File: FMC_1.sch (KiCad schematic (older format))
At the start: 14 parts, among them J5 SAMTEC_ASP-134603-01

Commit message: bugs fixed, silkscreen edited
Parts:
- renumbered J5 to P1
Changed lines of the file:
@@
 $EndComp
 $Comp
-L SAMTEC:SAMTEC_ASP-134603-01 J5
+L SAMTEC:SAMTEC_ASP-134603-01 P1
 U 1 1 5CF32820
 P 3750 1550
-F 0 "J5" H 4077 -500 50  0000 L CNN
+F 0 "P1" H 4077 -500 50  0000 L CNN
 F 1 "SAMTEC_ASP-134603-01" H 3750 -2640 60  0001 L CNN
 F 2 "SAMTEC_ASP-134603-01" H 3750 -3540 60  0001 L CNN
@@
 $EndComp
 $Comp
-L SAMTEC:SAMTEC_ASP-134603-01 J5
+L SAMTEC:SAMTEC_ASP-134603-01 P1
 U 2 1 5CF32A89
 P 6050 1550
-F 0 "J5" H 6378 -500 50  0000 L CNN
+F 0 "P1" H 6378 -500 50  0000 L CNN
 F 1 "SAMTEC_ASP-134603-01" H 6050 -2640 60  0001 L CNN
 F 2 "SAMTEC_ASP-134603-01" H 6050 -3540 60  0001 L CNN
@@
 $EndComp
 $Comp
-L SAMTEC:SAMTEC_ASP-134603-01 J5
+L SAMTEC:SAMTEC_ASP-134603-01 P1
 U 3 1 5CF32CEE
 P 8800 1550
-F 0 "J5" H 9128 -500 50  0000 L CNN
+F 0 "P1" H 9128 -500 50  0000 L CNN
 F 1 "SAMTEC_ASP-134603-01" H 8800 -2640 60  0001 L CNN
 F 2 "SAMTEC_ASP-134603-01" H 8800 -3540 60  0001 L CNN
@@
 $EndComp
 $Comp
-L SAMTEC:SAMTEC_ASP-134603-01 J5
+L SAMTEC:SAMTEC_ASP-134603-01 P1
 U 4 1 5CF32F53
 P 11450 1550
-F 0 "J5" H 11778 -500 50  0000 L CNN
+F 0 "P1" H 11778 -500 50  0000 L CNN
 F 1 "SAMTEC_ASP-134603-01" H 11450 -2640 60  0001 L CNN
 F 2 "SAMTEC_ASP-134603-01" H 11450 -3540 60  0001 L CNN

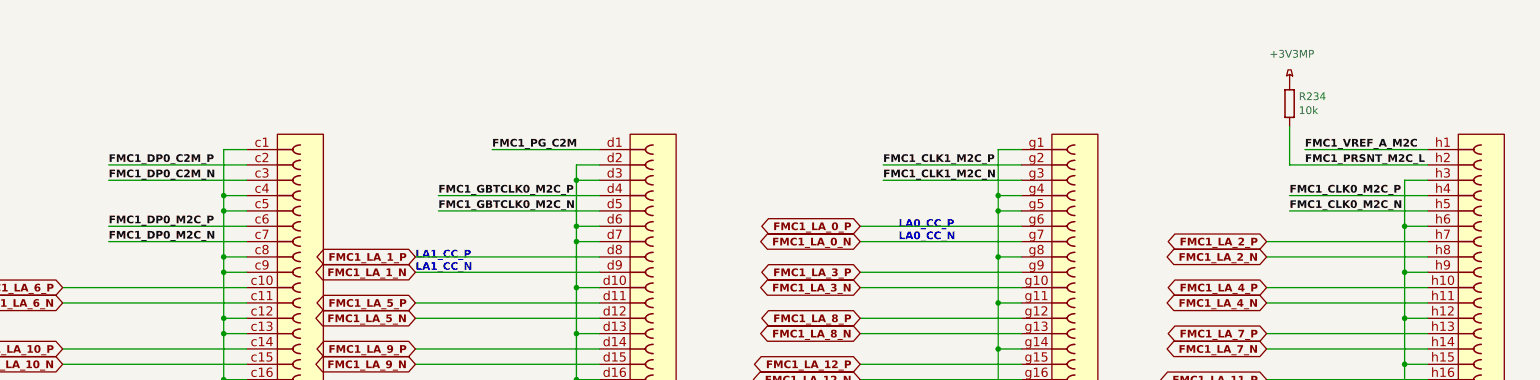
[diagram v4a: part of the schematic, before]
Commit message: new FMC JTAG chain
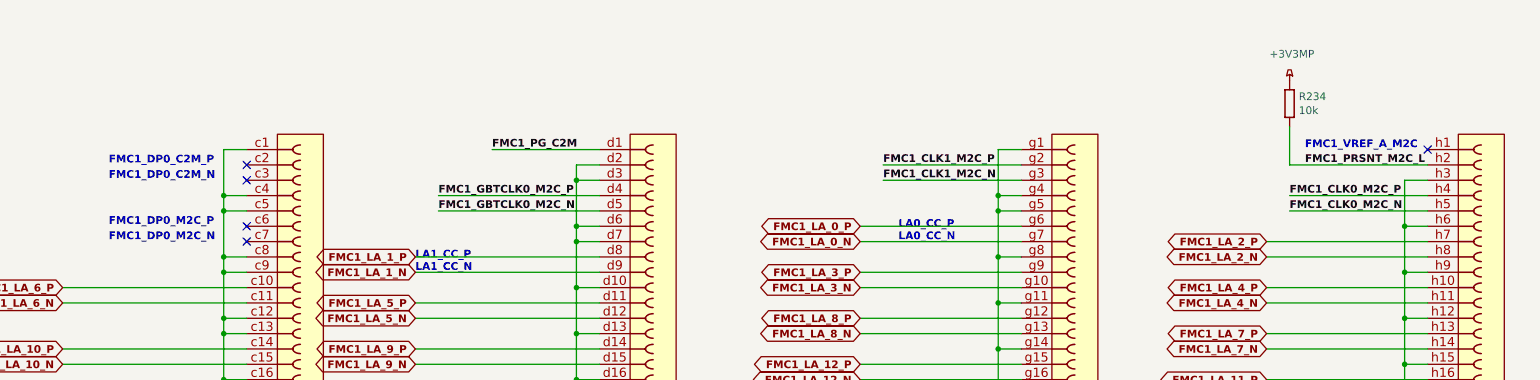
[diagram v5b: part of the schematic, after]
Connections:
- net FMC1_DP0_C2M_N: no longer names the net of P1.c3
- net FMC1_DP0_C2M_P: no longer names the net of P1.c2
- net FMC1_DP0_M2C_N: no longer names the net of P1.c7
- net FMC1_DP0_M2C_P: no longer names the net of P1.c6
- net FMC1_VREF_A_M2C: no longer names the net of P1.h1
- no-connect marks 0 -> 5
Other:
- note added: "FMC1_DP0_C2M_N"
- note added: "FMC1_DP0_C2M_P"
- note added: "FMC1_DP0_M2C_N"
- note added: "FMC1_DP0_M2C_P"
- note added: "FMC1_VREF_A_M2C"
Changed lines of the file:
@@
 Wire Wire Line
 	11100 5150 11100 5450
-Text Label 2650 1750 0    50   ~ 10
-FMC1_DP0_C2M_P
-Text Label 2650 1850 0    50   ~ 10
-FMC1_DP0_C2M_N
-Text Label 2650 2150 0    50   ~ 10
-FMC1_DP0_M2C_P
-Text Label 2650 2250 0    50   ~ 10
-FMC1_DP0_M2C_N
 Text Label 2850 4550 0    50   ~ 10
 I2C_FMC1_SCL
@@
 Wire Wire Line
 	2850 4650 3550 4650
-Wire Wire Line
-	2650 1750 3550 1750
-Wire Wire Line
-	2650 1850 3550 1850
-Wire Wire Line
-	2650 2150 3550 2150
-Wire Wire Line
-	2650 2250 3550 2250
 Text Notes 2400 3850 0    50   ~ 10
 LA18_CC_P\nLA18_CC_N
@@
 Text Label 5150 4850 0    50   ~ 10
 FMC1_TMS
-Text Label 5150 4950 0    50   ~ 10
-FMC1_TRST
 Text Label 5150 5050 0    50   ~ 10
 GA1_1
@@
 Wire Wire Line
 	5150 4850 5850 4850
-Wire Wire Line
-	5150 4950 5850 4950
 Wire Wire Line
 	5150 5050 5850 5050
@@
 Text Label 7700 1850 0    50   ~ 10
 FMC1_CLK1_M2C_N
-Text Label 10450 1650 0    50   ~ 10
-FMC1_VREF_A_M2C
 Text Label 10450 1750 0    50   ~ 10
 FMC1_PRSNT_M2C_L
@@
 Wire Wire Line
 	7700 1850 8600 1850
-Wire Wire Line
-	10450 1650 11250 1650
 Wire Wire Line
 	10350 1950 11250 1950
@@
 	-1   0    0    1
 $EndComp
+NoConn ~ 11250 1650
+Text Notes 10450 1650 0    50   ~ 10
+FMC1_VREF_A_M2C
+NoConn ~ 3550 1750
+NoConn ~ 3550 1850
+NoConn ~ 3550 2150
+NoConn ~ 3550 2250
+Text Notes 2650 1750 0    50   ~ 10
+FMC1_DP0_C2M_P
+Text Notes 2650 1850 0    50   ~ 10
+FMC1_DP0_C2M_N
+Text Notes 2650 2150 0    50   ~ 10
+FMC1_DP0_M2C_P
+Text Notes 2650 2250 0    50   ~ 10
+FMC1_DP0_M2C_N
+Text Label 5150 4950 0    50   ~ 10
+FMC1_TRST
+Wire Wire Line
+	5150 4950 5850 4950
 $EndSCHEMATC

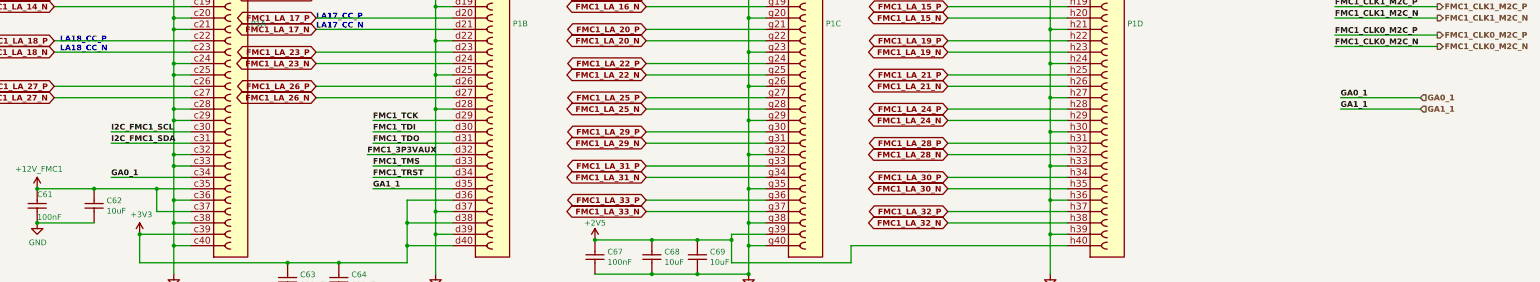
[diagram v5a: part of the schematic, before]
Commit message: JTAG improvrmrnt, bugs fixed
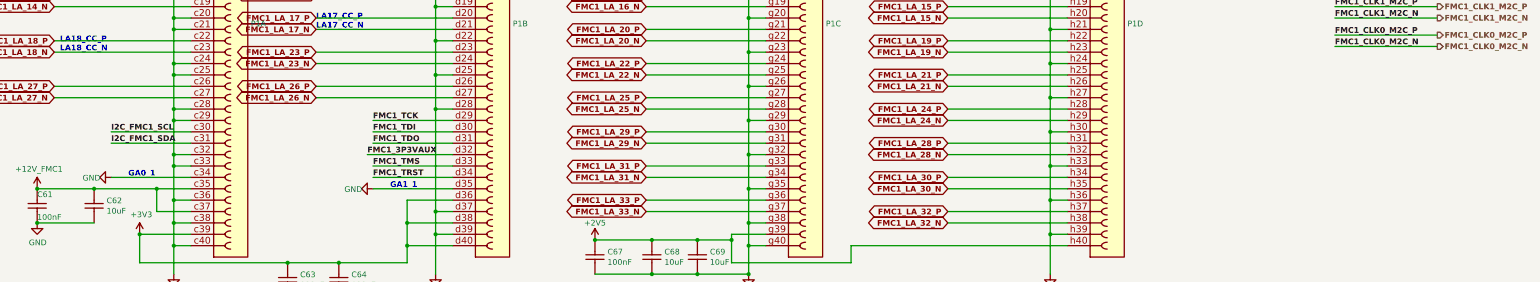
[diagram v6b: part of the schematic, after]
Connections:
- net GA0_1 is gone; now on net GND: P1.c34
- net GA1_1 is gone; now on net GND: P1.d35
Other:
- note added: "GA0_1"
- note added: "GA1_1"
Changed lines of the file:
@@
 Comment1 ""
 Comment2 ""
-Comment3 ""
+Comment3 "FMC 1 connector"
 Comment4 ""
 $EndDescr
@@
 Text Label 2850 4650 0    50   ~ 10
 I2C_FMC1_SDA
-Text Label 2850 4950 0    50   ~ 10
-GA0_1
 Wire Wire Line
 	3550 5050 3250 5050
@@
 Text Label 5150 4850 0    50   ~ 10
 FMC1_TMS
-Text Label 5150 5050 0    50   ~ 10
-GA1_1
 Wire Wire Line
 	5150 1650 5850 1650
@@
 Wire Wire Line
 	13600 3800 14500 3800
-Text Label 13650 4250 0    50   ~ 10
-GA0_1
-Wire Wire Line
-	13650 4250 14350 4250
-Text Label 13650 4350 0    50   ~ 10
-GA1_1
-Wire Wire Line
-	13650 4350 14350 4350
 Text HLabel 14500 3200 2    50   Output ~ 10
 FMC1_GBTCLK0_M2C_P
@@
 	1    0    0    -1
 $EndComp
-Text HLabel 14350 4250 2    50   Input ~ 10
-GA0_1
-Text HLabel 14350 4350 2    50   Input ~ 10
-GA1_1
 $Comp
 L power:+3.3VP #PWR?
@@
 Wire Wire Line
 	5150 4950 5850 4950
+$Comp
+L power:GND #PWR?
+U 1 1 5D17E89A
+P 2850 4950
+AR Path="/5BD32060/5D17E89A" Ref="#PWR?"  Part="1"
+AR Path="/5BD31F9A/5D17E89A" Ref="#PWR?"  Part="1"
+AR Path="/5BD31F9F/5D17E89A" Ref="#PWR?"  Part="1"
+AR Path="/5D17E89A" Ref="#PWR?"  Part="1"
+F 0 "#PWR?" H 2850 4700 50  0001 C CNN
+F 1 "GND" V 2855 4777 50  0000 C CNN
+F 2 "" H 2850 4950 50  0001 C CNN
+F 3 "" H 2850 4950 50  0001 C CNN
+	1    2850 4950
+	0    1    1    0
+$EndComp
+$Comp
+L power:GND #PWR?
+U 1 1 5D19449D
+P 5150 5050
+AR Path="/5BD32060/5D19449D" Ref="#PWR?"  Part="1"
+AR Path="/5BD31F9A/5D19449D" Ref="#PWR?"  Part="1"
+AR Path="/5BD31F9F/5D19449D" Ref="#PWR?"  Part="1"
+AR Path="/5D19449D" Ref="#PWR?"  Part="1"
+F 0 "#PWR?" H 5150 4800 50  0001 C CNN
+F 1 "GND" V 5155 4877 50  0000 C CNN
+F 2 "" H 5150 5050 50  0001 C CNN
+F 3 "" H 5150 5050 50  0001 C CNN
+	1    5150 5050
+	0    1    1    0
+$EndComp
+Text Notes 3000 4950 0    50   ~ 10
+GA0_1
+Text Notes 5300 5050 0    50   ~ 10
+GA1_1
 $EndSCHEMATC
